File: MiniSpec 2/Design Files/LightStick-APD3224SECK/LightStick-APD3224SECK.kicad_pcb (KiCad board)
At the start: 2 copper layers, 14 x 25 mm, 3 parts, among them IC1 AL5809-20P1-7, J1 TSM-104-02-S-DV-P-TR

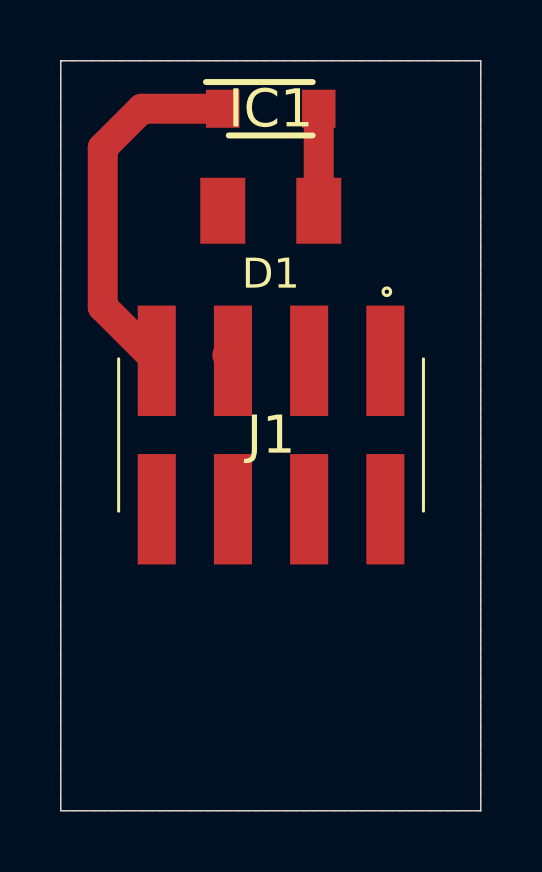
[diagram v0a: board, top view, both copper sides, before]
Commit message: big updates for 2 layer design with vias
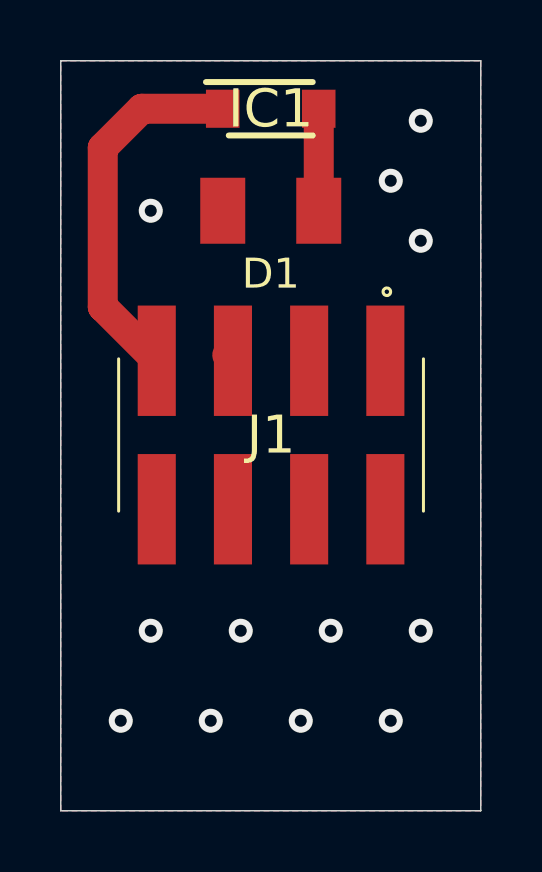
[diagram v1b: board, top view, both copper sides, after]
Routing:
- net GND: vias 0 -> 12
- added copper zone on B.Cu, net GND
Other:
- board text added: "APD Light"
- board text added: "Light APD"
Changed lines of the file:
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@@
-(kicad_pcb (version 20171130) (host pcbnew "(5.1.6)-1")
+(kicad_pcb (version 20171130) (host pcbnew "(5.1.9)-1")
   (general
     (thickness 1.6)
-    (drawings 27)
-    (tracks 7)
+    (drawings 29)
+    (tracks 19)
     (zones 0)
     (modules 3)
@@
   (layers
     (0 F.Cu signal)
-    (31 B.Cu signal hide)
+    (31 B.Cu signal)
     (32 B.Adhes user hide)
     (33 F.Adhes user hide)
@@
     (36 B.SilkS user hide)
     (37 F.SilkS user hide)
-    (38 B.Mask user hide)
-    (39 F.Mask user hide)
+    (38 B.Mask user)
+    (39 F.Mask user)
     (40 Dwgs.User user hide)
     (41 Cmts.User user hide)
     (42 Eco1.User user hide)
     (43 Eco2.User user hide)
-    (44 Edge.Cuts user)
+    (44 Edge.Cuts user hide)
     (45 Margin user hide)
     (46 B.CrtYd user hide)
@@
   )
   (setup
-    (last_trace_width 1)
+    (last_trace_width 0.25)
     (user_trace_width 0.6)
     (user_trace_width 1)
@@
     (visible_elements 7FFFFFFF)
     (pcbplotparams
-      (layerselection 0x00000_7fffffff)
+      (layerselection 0x3ffff_ffffffff)
       (usegerberextensions false)
       (usegerberattributes true)
@@
       (hpglpenspeed 20)
       (hpglpendiameter 15.000000)
-      (psnegative true)
+      (psnegative false)
       (psa4output false)
       (plotreference false)
@@
       (padsonsilk false)
       (subtractmaskfromsilk false)
-      (outputformat 4)
+      (outputformat 1)
       (mirror false)
       (drillshape 0)
       (scaleselection 1)
-      (outputdirectory ""))
+      (outputdirectory "../../../../../../Desktop/Temp MiniSpec/"))
   )
   (net 0 "")
@@
     (add_net GND)
     (add_net "Net-(D1-Pad2)")
-    (add_net SCL)
-    (add_net SDA)
   )
   (module SamacSys_Parts:TSM-104-YY-ZZZ-DV-P-TR (layer F.Cu)
@@
       (effects (font (size 1.27 1.27) (thickness 0.254)))
     )
-    (fp_text value TSM-104-02-S-DV-P-TR (at 0 0) (layer F.SilkS) hide
-      (effects (font (size 1.27 1.27) (thickness 0.254)))
-    )
+    (fp_text value TSM-104-02-S-DV-P-TR (at -8.01 0.525 90) (layer F.SilkS) hide
+      (effects (font (size 1.27 1.27) (thickness 0.254)))
+    )
+    (fp_line (start -5.08 -2.54) (end 5.08 -2.54) (layer Dwgs.User) (width 0.2))
+    (fp_line (start 5.08 -2.54) (end 5.08 2.54) (layer Dwgs.User) (width 0.2))
+    (fp_line (start 5.08 2.54) (end -5.08 2.54) (layer Dwgs.User) (width 0.2))
+    (fp_line (start -5.08 2.54) (end -5.08 -2.54) (layer Dwgs.User) (width 0.2))
+    (fp_line (start 5.08 -2.54) (end 5.08 2.54) (layer F.SilkS) (width 0.1))
+    (fp_line (start -5.08 2.54) (end -5.08 -2.54) (layer F.SilkS) (width 0.1))
+    (fp_line (start -6.28 -5.875) (end 6.28 -5.875) (layer Dwgs.User) (width 0.05))
+    (fp_line (start 6.28 -5.875) (end 6.28 5.315) (layer Dwgs.User) (width 0.05))
+    (fp_line (start 6.28 5.315) (end -6.28 5.315) (layer Dwgs.User) (width 0.05))
+    (fp_line (start -6.28 5.315) (end -6.28 -5.875) (layer Dwgs.User) (width 0.05))
     (fp_circle (center 3.86 -4.775) (end 3.81 -4.775) (layer F.SilkS) (width 0.254))
-    (fp_line (start -6.28 5.315) (end -6.28 -5.875) (layer Dwgs.User) (width 0.05))
-    (fp_line (start 6.28 5.315) (end -6.28 5.315) (layer Dwgs.User) (width 0.05))
-    (fp_line (start 6.28 -5.875) (end 6.28 5.315) (layer Dwgs.User) (width 0.05))
-    (fp_line (start -6.28 -5.875) (end 6.28 -5.875) (layer Dwgs.User) (width 0.05))
-    (fp_line (start -5.08 2.54) (end -5.08 -2.54) (layer F.SilkS) (width 0.1))
-    (fp_line (start 5.08 -2.54) (end 5.08 2.54) (layer F.SilkS) (width 0.1))
-    (fp_line (start -5.08 2.54) (end -5.08 -2.54) (layer Dwgs.User) (width 0.2))
-    (fp_line (start 5.08 2.54) (end -5.08 2.54) (layer Dwgs.User) (width 0.2))
-    (fp_line (start 5.08 -2.54) (end 5.08 2.54) (layer Dwgs.User) (width 0.2))
-    (fp_line (start -5.08 -2.54) (end 5.08 -2.54) (layer Dwgs.User) (width 0.2))
     (pad 8 smd rect (at -3.81 2.475) (size 1.27 3.68) (layers F.Cu F.Paste F.Mask)
       (net 1 GND))
@@
       (effects (font (size 1.27 1.27) (thickness 0.254)))
     )
-    (fp_text value AL5809-20P1-7 (at 0 0) (layer F.SilkS) hide
-      (effects (font (size 1.27 1.27) (thickness 0.254)))
-    )
+    (fp_text value AL5809-20P1-7 (at 0 -2.6) (layer F.SilkS) hide
+      (effects (font (size 1.27 1.27) (thickness 0.254)))
+    )
+    (fp_line (start -2.31 -1.115) (end 2.31 -1.115) (layer Dwgs.User) (width 0.05))
+    (fp_line (start 2.31 -1.115) (end 2.31 1.115) (layer Dwgs.User) (width 0.05))
+    (fp_line (start 2.31 1.115) (end -2.31 1.115) (layer Dwgs.User) (width 0.05))
+    (fp_line (start -2.31 1.115) (end -2.31 -1.115) (layer Dwgs.User) (width 0.05))
+    (fp_line (start -1.4 -0.89) (end 1.4 -0.89) (layer Dwgs.User) (width 0.1))
+    (fp_line (start 1.4 -0.89) (end 1.4 0.89) (layer Dwgs.User) (width 0.1))
+    (fp_line (start 1.4 0.89) (end -1.4 0.89) (layer Dwgs.User) (width 0.1))
+    (fp_line (start -1.4 0.89) (end -1.4 -0.89) (layer Dwgs.User) (width 0.1))
+    (fp_line (start -1.4 -0.33) (end -0.84 -0.89) (layer Dwgs.User) (width 0.1))
+    (fp_line (start -2.16 -0.89) (end 1.4 -0.89) (layer F.SilkS) (width 0.2))
     (fp_line (start -1.4 0.89) (end 1.4 0.89) (layer F.SilkS) (width 0.2))
-    (fp_line (start -2.16 -0.89) (end 1.4 -0.89) (layer F.SilkS) (width 0.2))
-    (fp_line (start -1.4 -0.33) (end -0.84 -0.89) (layer Dwgs.User) (width 0.1))
-    (fp_line (start -1.4 0.89) (end -1.4 -0.89) (layer Dwgs.User) (width 0.1))
-    (fp_line (start 1.4 0.89) (end -1.4 0.89) (layer Dwgs.User) (width 0.1))
-    (fp_line (start 1.4 -0.89) (end 1.4 0.89) (layer Dwgs.User) (width 0.1))
-    (fp_line (start -1.4 -0.89) (end 1.4 -0.89) (layer Dwgs.User) (width 0.1))
-    (fp_line (start -2.31 1.115) (end -2.31 -1.115) (layer Dwgs.User) (width 0.05))
-    (fp_line (start 2.31 1.115) (end -2.31 1.115) (layer Dwgs.User) (width 0.05))
-    (fp_line (start 2.31 -1.115) (end 2.31 1.115) (layer Dwgs.User) (width 0.05))
-    (fp_line (start -2.31 -1.115) (end 2.31 -1.115) (layer Dwgs.User) (width 0.05))
     (pad 2 smd rect (at 1.6 0) (size 1.12 1.27) (layers F.Cu F.Paste F.Mask)
       (net 2 "Net-(D1-Pad2)"))
@@
     (pad 1 smd rect (at -1.6 0) (size 1.5 2.2) (layers F.Cu F.Paste F.Mask)
       (net 1 GND))
+  )
+  (gr_text "APD Light" (at 145 86) (layer B.Mask)
+    (effects (font (size 1 1) (thickness 0.15)) (justify mirror))
+  )
+  (gr_text "Light APD" (at 145 86) (layer B.SilkS)
+    (effects (font (size 1 1) (thickness 0.15)) (justify mirror))
   )
   (gr_line (start 201 168) (end 201 73) (layer Eco2.User) (width 0.15))
@@
   (segment (start 143.55 84.81) (end 143.74 85) (width 1) (layer F.Cu) (net 1))
   (segment (start 143.6 84.86) (end 143.74 85) (width 1) (layer F.Cu) (net 1))
+  (via (at 150 77) (size 0.8) (drill 0.4) (layers F.Cu B.Cu) (net 1))
+  (via (at 149 79) (size 0.8) (drill 0.4) (layers F.Cu B.Cu) (net 1))
+  (via (at 150 81) (size 0.8) (drill 0.4) (layers F.Cu B.Cu) (net 1))
+  (via (at 141 94) (size 0.8) (drill 0.4) (layers F.Cu B.Cu) (net 1))
+  (via (at 144 94) (size 0.8) (drill 0.4) (layers F.Cu B.Cu) (net 1))
+  (via (at 147 94) (size 0.8) (drill 0.4) (layers F.Cu B.Cu) (net 1))
+  (via (at 150 94) (size 0.8) (drill 0.4) (layers F.Cu B.Cu) (net 1))
+  (via (at 140 97) (size 0.8) (drill 0.4) (layers F.Cu B.Cu) (net 1))
+  (via (at 143 97) (size 0.8) (drill 0.4) (layers F.Cu B.Cu) (net 1))
+  (via (at 146 97) (size 0.8) (drill 0.4) (layers F.Cu B.Cu) (net 1))
+  (via (at 149 97) (size 0.8) (drill 0.4) (layers F.Cu B.Cu) (net 1))
+  (via (at 141 80) (size 0.8) (drill 0.4) (layers F.Cu B.Cu) (net 1))
   (segment (start 146.6 80) (end 146.6 76.6) (width 1) (layer F.Cu) (net 2))
   (segment (start 143.4 76.6) (end 140.7 76.6) (width 1) (layer F.Cu) (net 3))
@@
     (connect_pads (clearance 0.508))
     (min_thickness 0.254)
+    (fill yes (arc_segments 32) (thermal_gap 0.508) (thermal_bridge_width 0.508))
+    (polygon
+      (pts
+        (xy 152 100) (xy 138 100) (xy 138 75) (xy 152 75)
+      )
+    )
+  )
+  (zone (net 1) (net_name GND) (layer B.Cu) (hatch edge 0.508)
+    (connect_pads (clearance 0.508))
+    (min_thickness 0.254)

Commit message: added phone jack port for 25mm tube base
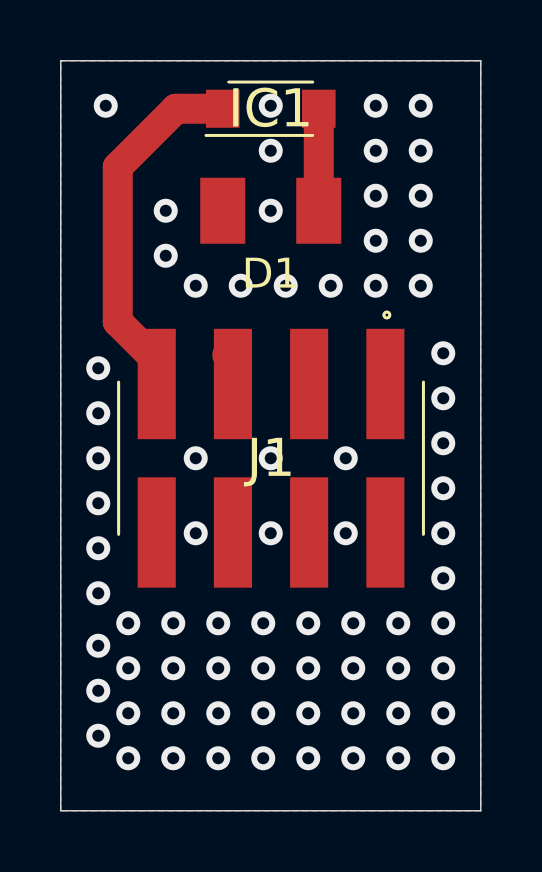
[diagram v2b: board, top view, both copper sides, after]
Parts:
- IC1: footprint SamacSys_Parts:SODFL3718X100N -> BinomicaLabs:AL580920QP17
- J1: footprint SamacSys_Parts:TSM-104-YY-ZZZ-DV-P-TR -> BinomicaLabs:TSM-104-YY-ZZZ-DV-P-TR
- moved J1 0.78 mm to (145.0, 88.2)
- turned IC1 to 180 degrees
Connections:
- J1 pad 1: (no net) -> SDA
- J1 pad 3: (no net) -> SCL
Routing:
- net +3V3: track 12.4 -> 11.3 mm
- net GND: vias 12 -> 73
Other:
- net class Default removed
- board text removed: "Light APD"
